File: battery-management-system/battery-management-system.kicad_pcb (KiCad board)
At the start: 4 copper layers, 100 x 111 mm, 212 parts, among them J1 CELL4_PLUS, J10 18V, J11 3V3, J12 AMPHENOL_micro_usb_10118194-0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, J13 I2C, J14 UART_INTERCONNECT, J15 LEDS, J16 CHARGE/DISCHARGE, J17 UART_USB, J18 rspro_header_5pin_3_5mm, J19 TEMP_CELL1, J2 CELL4_MINUS, J20 TEMP_CELL2, J21 TEMP_CELL3, J22 TEMP_CELL4, J23 Conn_01x05, J24 Charge, J25 Discharge, J3 CELL3_MINUS, J4 CELL2_MINUS, J5 CELL1_MINUS, J6 VBAT+, J7 VBAT+_CHARGE, J8 VBAT-, J9 5V, Q1 DMN3404L, Q10 DMN3404L, Q11 BS250FTA, Q12 BS250FTA, Q13 BS250FTA, Q14 BS250FTA, Q15 BS250FTA, Q16 DMN3404L, Q17 DMN3404L, Q18 DMN3404L, Q19 DMN3404L, Q2 TJ40S04M3L, Q20 DMN3404L, Q21 DMN3404L, Q22 DMN3404L, Q23 DMN3404L, Q24 DMN3404L, Q25 DMN3404L, Q26 DMN3404L, Q27 DMN3404L, Q28 DMN3404L, Q29 DMN3404L, Q3 TJ40S04M3L, Q30 DMN3404L, Q31 DMN3404L, Q32 DMN3404L, Q33 DMN3404L, Q34 DMN3404L, Q35 DMN3404L, Q36 DMN3404L, Q37 DMN3404L, Q38 DMN3404L, Q39 DMN3404L, Q4 DMN3404L, Q40 TJ40S04M3L, Q5 DMN3404L, Q6 DMN3404L, Q7 DMN3404L, Q8 DMN3404L, Q9 DMN3404L, U1 ICL7660, U10 STM32L071CZTx, U11 LM2904M8-13, U12 LM2904M8-13, U13 MC74VHC139, U2 L6982C33DR, U3 L6982C33DR, U4 ICL7660, U5 FT230XS, U6 ARM-JTAG-SWD, U7 AT24C512C, U8 NCT75DR2G, U9 STC3100

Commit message: place USB again
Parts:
- moved C13 40.8 mm to (42.2, 111.0)
- moved C15 40.1 mm to (40.5, 111.2), turned to 90 degrees
- moved C14 38.5 mm to (27.5, 112.8), turned to 180 degrees
- moved C17 38.5 mm to (39.0, 111.2), turned to 90 degrees
- moved C19 36.8 mm to (27.5, 114.2), turned to 180 degrees
- moved J17 33.9 mm to (40.2, 116.8), turned to -90 degrees
- moved U5 33.8 mm to (34.0, 111.1), turned to -90 degrees
- moved D17 31.8 mm to (21.8, 101.8), turned to 90 degrees
- moved J12 30.9 mm to (21.6, 108.0)
- moved FB1 30.2 mm to (27.5, 104.8)
- moved C16 30.1 mm to (27.5, 111.2)
- moved C18 30.1 mm to (27.5, 106.4)
- moved R17 30.1 mm to (27.5, 108.0)
- moved R18 30.1 mm to (27.5, 109.6)
- moved D18 30.1 mm to (24.0, 101.8), turned to 90 degrees
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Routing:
- net GND: track 143.9 -> 117.9 mm, vias 29 -> 26
- net Net-(D18-K): track 20.4 -> 0.00 mm
- net /5V_EXT: track 1.15 -> 20.7 mm, vias 1 -> 2
- net /MCU/UART_USB_TX: track 18.8 -> 0.00 mm, vias 2 -> 0
- net /PACK_EXT: track 89.8 -> 104.5 mm
- net Net-(D17-K): track 14.5 -> 0.00 mm
- net Net-(U5-3V3OUT): track 13.1 -> 0.00 mm
- net /MCU/UART_USB_RX: track 12.5 -> 0.00 mm, vias 2 -> 0
- net Net-(U5-USBDM): track 10.9 -> 0.00 mm
- net Net-(U5-USBDP): track 7.53 -> 0.00 mm
- net /3V3: track 19.9 -> 14.8 mm, vias 4 -> 3
- net Net-(J12-VCC): track 4.40 -> 0.00 mm
- net Net-(J12-D+): track 3.97 -> 0.00 mm
- net /5V_USB: track 17.9 -> 21.7 mm
- net Net-(U5-~{CTS}): track 3.77 -> 0.00 mm, vias 2 -> 0
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
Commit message: continue with layout
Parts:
- R38, R39: moved to F.Cu
- moved R39 138.9 mm to (44.2, 117.0)
- moved R38 138.9 mm to (44.2, 115.2)
- moved C26 138.0 mm to (79.0, 95.5), turned to 180 degrees
- moved R37 136.4 mm to (61.8, 100.2)
- moved R34 134.3 mm to (60.5, 100.2)
- moved R32 133.9 mm to (59.2, 100.2)
- moved C22 131.1 mm to (53.2, 104.2), turned to 180 degrees
- moved R29 121.2 mm to (79.0, 94.0), turned to 0 degrees
- moved C21 117.6 mm to (53.8, 116.0), turned to -90 degrees
- moved C24 116.0 mm to (56.5, 115.5)
- moved J16 103.4 mm to (51.8, 91.5), turned to 0 degrees
- moved C25 100.7 mm to (65.0, 100.2), turned to 90 degrees
- moved R36 81.7 mm to (111.5, 100.8), turned to 180 degrees
- moved R35 79.6 mm to (111.5, 102.5), turned to 180 degrees
- moved J13 53.5 mm to (91.5, 118.5)
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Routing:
- net /5V_EXT: track 20.7 -> 215.5 mm
- net /5V: track 40.4 -> 144.6 mm
- net /5V_USB: track 21.7 -> 77.5 mm, vias 2 -> 4
- net /MCU/UART_USB_RX: track 0.00 -> 28.7 mm
- net /MCU/UART_USB_TX: track 0.00 -> 21.9 mm, vias 0 -> 2
- net GND: track 117.9 -> 138.1 mm, vias 26 -> 30
- net Net-(D17-K): track 0.00 -> 18.8 mm, vias 0 -> 2
- net Net-(D18-K): track 0.00 -> 11.8 mm
- net Net-(U5-3V3OUT): track 0.00 -> 11.7 mm
- net Net-(U5-USBDM): track 0.00 -> 9.27 mm
- net Net-(U5-USBDP): track 0.00 -> 5.41 mm
- net /3V3: track 14.8 -> 19.9 mm, vias 3 -> 4
- net Net-(J12-VCC): track 0.00 -> 4.16 mm
- net Net-(U5-~{CTS}): track 0.00 -> 3.31 mm
- net Net-(J12-D+): track 0.00 -> 3.10 mm
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
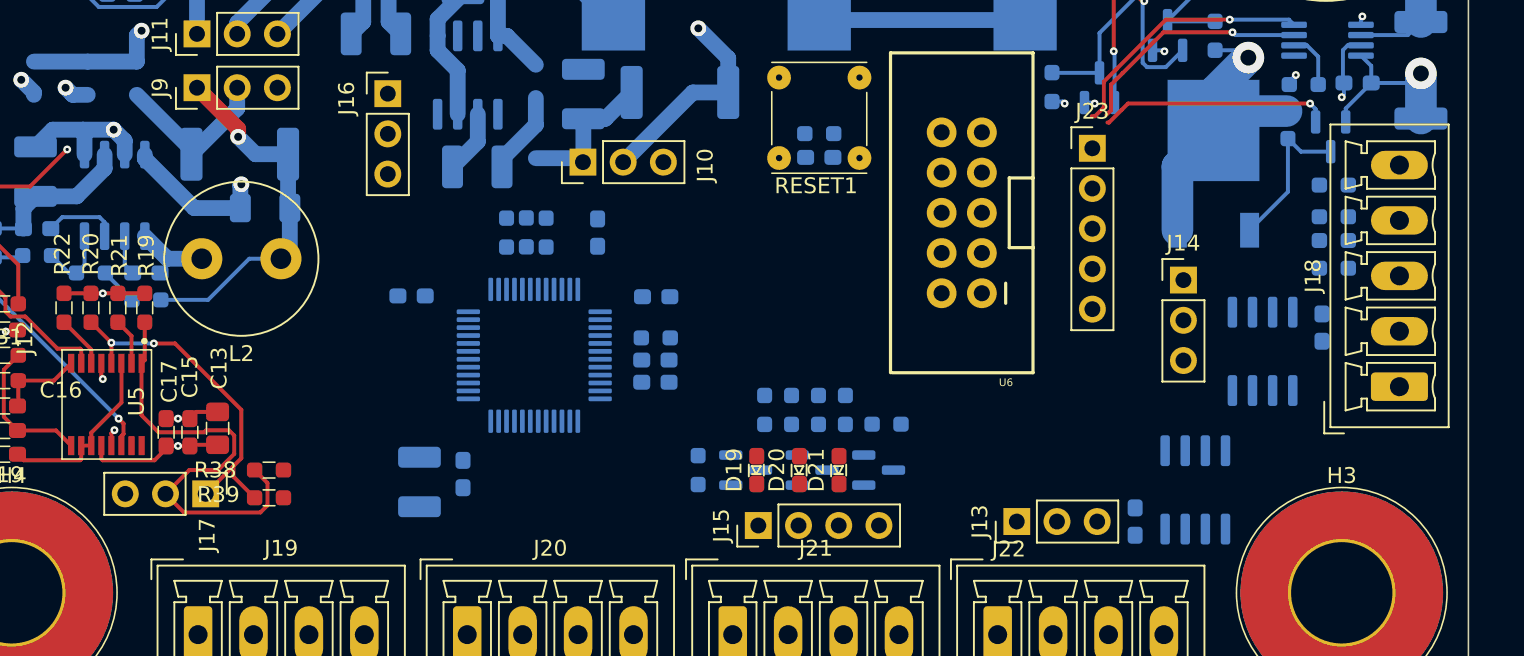
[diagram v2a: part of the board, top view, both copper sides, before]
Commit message: improve routing of power supply
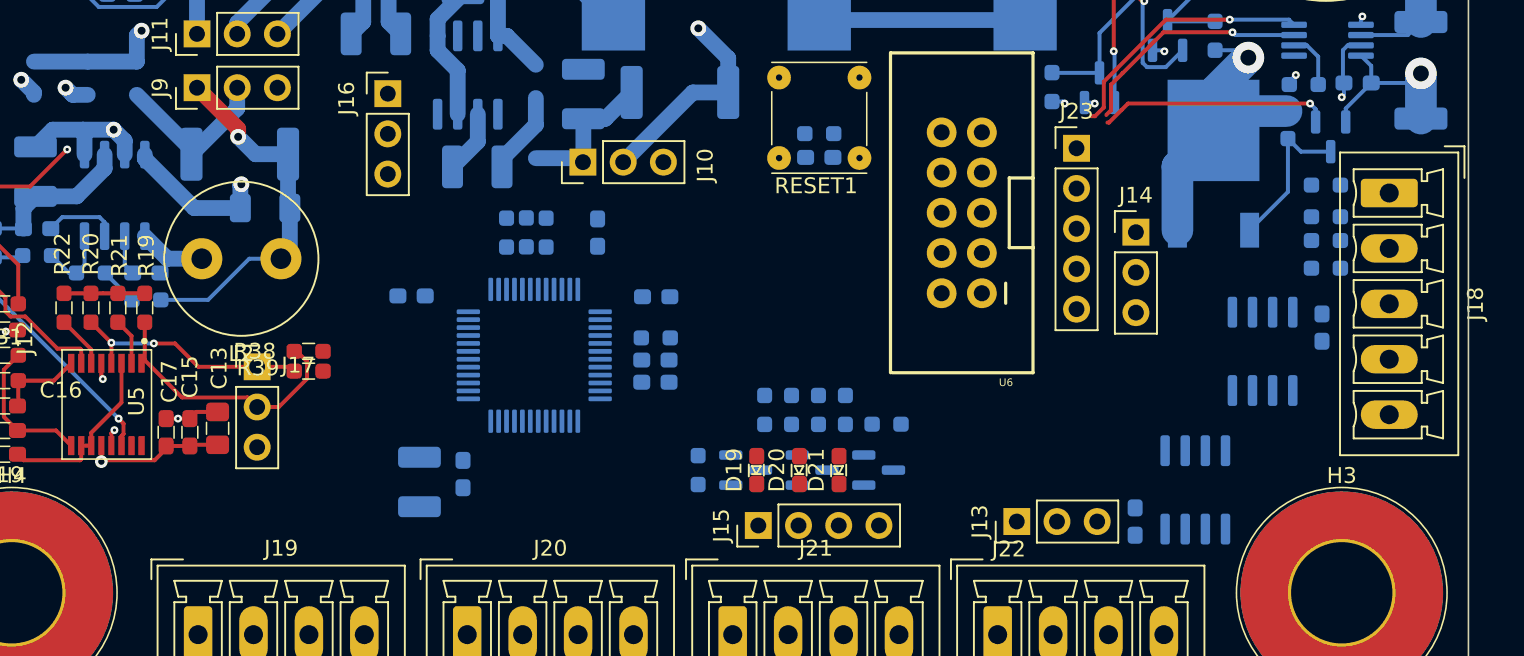
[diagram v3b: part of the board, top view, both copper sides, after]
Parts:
- moved J18 12.2 mm to (115.0, 97.8), turned to -90 degrees
- moved J17 8.66 mm to (43.5, 108.7), turned to 0 degrees
- moved R39 8.38 mm to (46.8, 109.0)
- moved R38 7.91 mm to (46.8, 107.8)
- moved J14 4.26 mm to (99.0, 100.2)
- moved J23 1.00 mm to (95.2, 94.9)
- moved R35 0.50 mm to (111.0, 102.5)
- moved R36 0.50 mm to (111.0, 100.8)
- moved R40 0.50 mm to (111.0, 99.2)
- moved R41 0.50 mm to (111.0, 97.2)
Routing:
- net /5V_EXT: track 215.5 -> 158.5 mm
- net /5V: track 144.6 -> 120.6 mm
- net /MCU/UART_USB_RX: track 28.7 -> 17.1 mm
- net /MCU/UART_USB_TX: track 21.9 -> 15.4 mm
- net /5V_USB: track 77.5 -> 75.0 mm
- net /3V3: vias 4 -> 3

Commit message: improve layout
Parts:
- moved J13 5.31 mm to (96.8, 118.8), turned to -90 degrees
- moved J14 5.05 mm to (99.0, 105.3), turned to 180 degrees
- moved J16 4.78 mm to (52.0, 96.2), turned to 180 degrees
- moved R35 4.75 mm to (111.0, 97.8)
- moved R41 3.50 mm to (111.0, 100.8)
- moved R36 1.75 mm to (111.0, 102.5)
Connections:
- U10 pad 2: /MCU/LED1 -> /MCU/LED3
- U10 pad 4: /MCU/LED3 -> /MCU/LED1
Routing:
- net /MCU/SDA: track 15.0 -> 101.9 mm
- net /MCU/SCL: track 16.5 -> 102.7 mm
- net GND: track 138.1 -> 202.8 mm, vias 30 -> 42
- net /3V3: track 19.9 -> 58.6 mm, vias 3 -> 13
- net /MCU/LED3: track 0.00 -> 27.0 mm
- net /Interconnect/UART_RX: track 0.00 -> 26.7 mm
- net /Interconnect/UART_TX: track 0.00 -> 26.3 mm
- net /MCU/LED2: track 0.00 -> 23.1 mm
- net /MCU/LED1: track 0.00 -> 20.1 mm
- net /MCU/NRST: track 0.00 -> 13.3 mm
- net Net-(D20-K): track 0.00 -> 6.08 mm, vias 0 -> 1
- net /MCU/VDDA: track 0.00 -> 5.62 mm
- net Net-(Q6-D): track 0.00 -> 5.27 mm
- net Net-(D21-K): track 0.00 -> 4.64 mm, vias 0 -> 1
- net Net-(D19-K): track 0.00 -> 4.22 mm, vias 0 -> 1
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
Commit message: improve layout
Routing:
- net /CELL_BALANCING_A0: track 13.0 -> 80.1 mm, vias 1 -> 3
- net /CELL_BALANCING_A1: track 13.3 -> 78.8 mm, vias 1 -> 3
- net Net-(U10-PB11): track 0.00 -> 63.2 mm, vias 0 -> 2
- net Net-(U10-PB10): track 0.00 -> 62.2 mm
- net /CELL_BALANCING_STROBE: track 62.9 -> 110.9 mm, vias 2 -> 4
- net /Cell Measurement/CELL3: track 13.0 -> 58.7 mm, vias 1 -> 3
- net /Battery Pack/CHARGE_AVAILABLE: track 27.7 -> 72.3 mm, vias 1 -> 2
- net /Cell Measurement/CELL1: track 16.5 -> 60.9 mm, vias 1 -> 3
- net /Cell Measurement/CELL4: track 39.5 -> 82.8 mm, vias 0 -> 1
- net /Cell Measurement/CELL2: track 35.2 -> 77.3 mm, vias 0 -> 1
- net /EN_CELL_BALANCING: track 14.6 -> 50.0 mm
- net /MCU/SDA: track 101.9 -> 136.0 mm, vias 1 -> 4
- net /MCU/SWCLK: track 0.00 -> 33.0 mm, vias 0 -> 1
- net /MCU/SWDIO: track 0.00 -> 31.8 mm, vias 0 -> 1
- net /MCU/SCL: track 102.7 -> 132.5 mm, vias 1 -> 3
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
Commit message: improve layout
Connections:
- U10 pad 20: /EN_CELL_MEASUREMENT -> unconnected-(U10-PB2-Pad20)
- U10 pad 26: unconnected-(U10-PB13-Pad26) -> /CHARGE
- U10 pad 27: unconnected-(U10-PB14-Pad27) -> /DISCHARGE
- U10 pad 33: unconnected-(U10-PA12-Pad33) -> /EN_CELL_MEASUREMENT
- U10 pad 39: /CHARGE -> unconnected-(U10-PB3-Pad39)
- U10 pad 40: /EN_CELL_BALANCING -> unconnected-(U10-PB4-Pad40)
- U10 pad 41: /DISCHARGE -> unconnected-(U10-PB5-Pad41)
- U10 pad 5: unconnected-(U10-PH0-Pad5) -> /EN_CELL_BALANCING
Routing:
- net /CHARGE: track 41.3 -> 80.9 mm
- net /DISCHARGE: track 37.5 -> 72.1 mm
- net /EN_CELL_MEASUREMENT: track 47.6 -> 64.6 mm, vias 0 -> 3
- net /EN_CELL_BALANCING: track 50.0 -> 61.0 mm, vias 1 -> 3
- net /MCU/NRST: track 37.1 -> 38.4 mm
- net /Cell Measurement/CELL3: track 58.7 -> 58.1 mm
- net /MCU/SWDIO: track 31.8 -> 31.3 mm

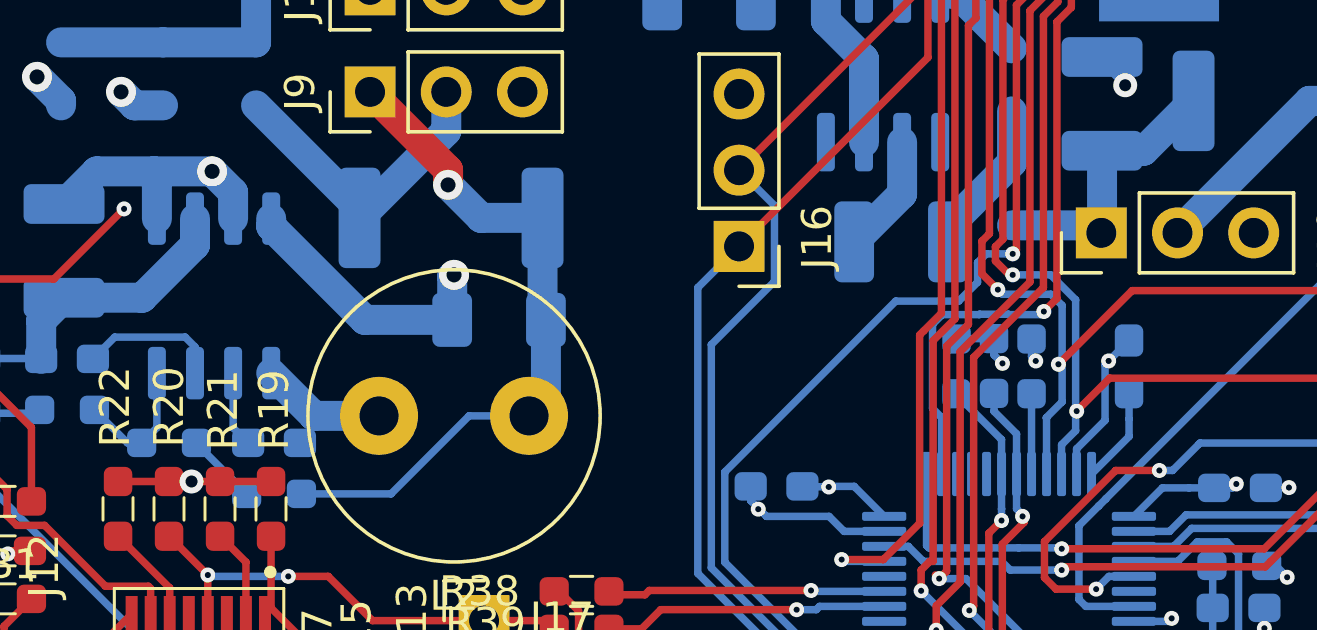
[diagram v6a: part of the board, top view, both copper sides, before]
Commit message: fix design rule errors
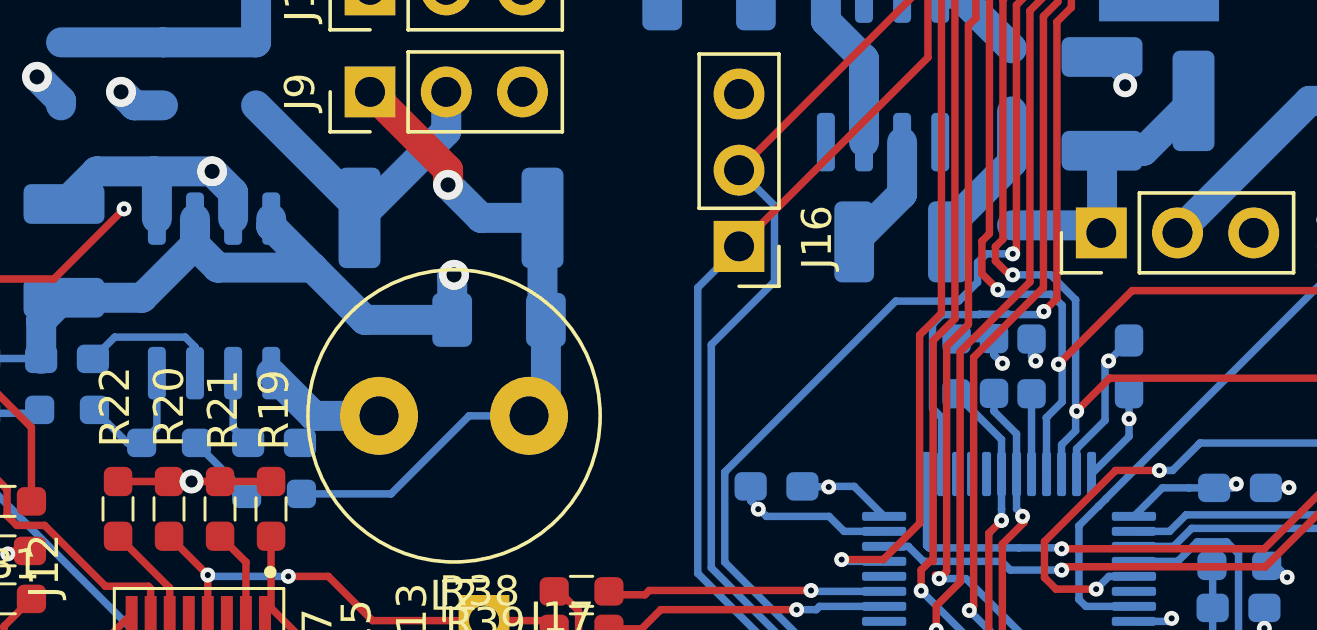
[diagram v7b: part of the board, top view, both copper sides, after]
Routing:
- net GND: track 202.0 -> 206.2 mm
- net /5V: track 122.6 -> 123.3 mm
- net /3V3: vias 14 -> 15
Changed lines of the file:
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@@
   (segment (start 106.365 105.275) (end 105.095 105.275) (width 0.25) (layer "B.Cu") (net 2))
   (segment (start 30.7 79.5125) (end 32.052499 79.5125) (width 0.25) (layer "B.Cu") (net 2))
+  (segment (start 33.865 96.199999) (end 34.622716 96.957715) (width 1) (layer "B.Cu") (net 2))
   (segment (start 56.4625 71.155) (end 56.4625 70.4) (width 0.25) (layer "B.Cu") (net 2))
   (segment (start 42.4375 98.7) (end 42.4375 97.2625) (width 1) (layer "B.Cu") (net 2))
   (segment (start 71.35 114.3375) (end 73.375 114.3375) (width 0.25) (layer "B.Cu") (net 2))
   (segment (start 78.15 111.65) (end 77.25 110.75) (width 0.25) (layer "B.Cu") (net 2))
-  (segment (start 33.865 96.199999) (end 33.865 95.325) (width 1) (layer "B.Cu") (net 2))
   (segment (start 81.8125 114.3) (end 82.6345 114.3) (width 0.25) (layer "B.Cu") (net 2))
   (segment (start 113.2125 87.125) (end 113.2125 86.6875) (width 0.25) (layer "B.Cu") (net 2))
+  (segment (start 39.52457 98.7) (end 37.782285 96.957715) (width 1) (layer "B.Cu") (net 2))
   (segment (start 52.6725 105.01) (end 52.70625 105.04375) (width 0.25) (layer "B.Cu") (net 2))
   (segment (start 112.25 93.2625) (end 112.25 92.4125) (width 0.25) (layer "B.Cu") (net 2))
@@
   (segment (start 51.9375 66.3375) (end 51.9 66.3) (width 0.25) (layer "B.Cu") (net 2))
   (segment (start 55.43 117.44) (end 55.43 117.4325) (width 0.25) (layer "B.Cu") (net 2))
+  (segment (start 37.782285 96.957715) (end 36.405 95.58043) (width 1) (layer "B.Cu") (net 2))
   (segment (start 102.115 118.975) (end 102.115 118.000001) (width 0.25) (layer "B.Cu") (net 2))
   (segment (start 64.1 89.9375) (end 63.929602 89.9375) (width 0.25) (layer "B.Cu") (net 2))
@@
   (segment (start 37.3 72.5375) (end 38.78125 74.01875) (width 1) (layer "B.Cu") (net 2))
   (segment (start 113.8625 89.725) (end 113.2125 89.075) (width 0.25) (layer "B.Cu") (net 2))
+  (segment (start 33.865 95.325) (end 33.865 96.199999) (width 1) (layer "B.Cu") (net 2))
   (segment (start 85.35 44.75) (end 85.4 44.7) (width 0.25) (layer "B.Cu") (net 2))
   (segment (start 77.6125 114.3) (end 78.15 113.7625) (width 0.25) (layer "B.Cu") (net 2))
@@
   (segment (start 69.51 108.98) (end 69.5125 108.9825) (width 0.25) (layer "B.Cu") (net 2))
   (segment (start 69.5625 104.3) (end 70.32 104.3) (width 0.25) (layer "B.Cu") (net 2))
+  (segment (start 34.622716 96.957715) (end 37.782285 96.957715) (width 1) (layer "B.Cu") (net 2))
   (segment (start 29.5 97.9625) (end 32.102499 97.9625) (width 1) (layer "B.Cu") (net 2))
   (segment (start 32.865 78.699999) (end 33.190001 79.025) (width 0.25) (layer "B.Cu") (net 2))
@@
   (segment (start 55.43 117.4325) (end 55.55625 117.30625) (width 0.25) (layer "B.Cu") (net 2))
   (segment (start 52.64 105.01) (end 52.6725 105.01) (width 0.25) (layer "B.Cu") (net 2))
-  (segment (start 39.52457 98.7) (end 36.405 95.58043) (width 1) (layer "B.Cu") (net 2))
   (segment (start 93.3 57.487) (end 94.5 58.687) (width 0.25) (layer "F.Cu") (net 3))
   (segment (start 93.3 55.0625) (end 93.3 57.487) (width 0.25) (layer "F.Cu") (net 3))
@@
   (via (at 55.47 114.63) (size 0.5) (drill 0.2) (layers "F.Cu" "B.Cu") (net 5))
   (via (at 76.2 56.9) (size 0.5) (drill 0.2) (layers "F.Cu" "B.Cu") (net 5))
+  (via (at 65 102) (size 0.5) (drill 0.2) (layers "F.Cu" "B.Cu") (net 5))
   (via (at 80.06 113.7) (size 0.5) (drill 0.2) (layers "F.Cu" "B.Cu") (net 5))
   (via (at 33.75 104.0875) (size 0.8) (drill 0.4) (layers "F.Cu" "B.Cu") (net 5))
@@
   (segment (start 112.1375 91.5625) (end 112 91.7) (width 0.25) (layer "B.Cu") (net 5))
   (segment (start 99.3375 118.975) (end 98.95 119.3625) (width 0.25) (layer "B.Cu") (net 5))
-  (segment (start 65 101.1125) (end 65 102) (width 0.25) (layer "B.Cu") (net 5))
   (segment (start 75.5 57.6) (end 76.2 56.9) (width 0.25) (layer "B.Cu") (net 5))
   (segment (start 99.975 118.975) (end 99.3375 118.975) (width 0.25) (layer "B.Cu") (net 5))
@@
   (segment (start 66.1125 104.3) (end 65.1625 105.25) (width 0.25) (layer "B.Cu") (net 5))
   (segment (start 67 104.3) (end 66.1125 104.3) (width 0.25) (layer "B.Cu") (net 5))
+  (segment (start 65 101.1125) (end 65 102) (width 0.25) (layer "B.Cu") (net 5))
   (segment (start 110.0875 99.25) (end 110.0875 100.75) (width 0.25) (layer "B.Cu") (net 5))
   (segment (start 56.5 114.6375) (end 55.4775 114.6375) (width 0.25) (layer "B.Cu") (net 5))
@@
   (via (at 49.991102 72.346398) (size 0.5) (drill 0.2) (layers "F.Cu" "B.Cu") (net 39))
   (via (at 36.2 87.5) (size 1) (drill 0.5) (layers "F.Cu" "B.Cu") (net 39))
+  (segment (start 43.492767 83.742767) (end 38.467233 83.742767) (width 2) (layer "In1.Cu") (net 39))
+  (segment (start 38.467233 83.742767) (end 36.2 86.01) (width 2) (layer "In1.Cu") (net 39))
   (segment (start 53.49857 77.244432) (end 86.004138 109.75) (width 2) (layer "In1.Cu") (net 39))
   (segment (start 86.004138 109.75) (end 100.25 109.75) (width 2) (layer "In1.Cu") (net 39))
-  (segment (start 41.585534 85.65) (end 38.05 85.65) (width 2) (layer "In1.Cu") (net 39))
   (segment (start 49.991102 77.244432) (end 49.991102 72.346398) (width 2) (layer "In1.Cu") (net 39))
   (segment (start 49.991102 77.244432) (end 53.49857 77.244432) (width 2) (layer "In1.Cu") (net 39))
   (segment (start 43.492767 83.742767) (end 49.991102 77.244432) (width 2) (layer "In1.Cu") (net 39))
   (segment (start 108.75 101.25) (end 115 101.25) (width 2) (layer "In1.Cu") (net 39))
-  (segment (start 38.05 85.65) (end 36.2 87.5) (width 2) (layer "In1.Cu") (net 39))
   (segment (start 100.25 109.75) (end 108.75 101.25) (width 2) (layer "In1.Cu") (net 39))
-  (segment (start 41.585534 85.65) (end 43.492767 83.742767) (width 2) (layer "In1.Cu") (net 39))
-  (segment (start 43.721905 83.742767) (end 43.492767 83.742767) (width 2) (layer "In1.Cu") (net 39))
+  (segment (start 36.2 86.01) (end 36.2 87.5) (width 2) (layer "In1.Cu") (net 39))
   (segment (start 35.9 89.45) (end 35.9 87.8) (width 1) (layer "B.Cu") (net 39))
   (segment (start 48.525 78.175) (end 49.5 77.2) (width 1) (layer "B.Cu") (net 39))
